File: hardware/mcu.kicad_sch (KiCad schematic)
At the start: 39 parts, among them J1 USB-C, SW3 RUN, SW4 BOOTSEL, U20 RP2350B, U21 GD25Q128ESIGR, U22 APS6404L-3SQR-SN, Y1 12MHz

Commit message: Plain address bytes in hardware; DVDD spine and bottom-row fan pre-routed
U1 delivers A0-A7 and U2 A8-A15 on MD0-MD7 (U2 over its fingers, U1 in the row
above fed from both sides), so the firmware sees ordinary addresses. preroute.py
now also fixes the DVDD spine under the package, the inner 3.3 V supply links,
pin 51's capacitor and a deterministic fan for the fully used bottom pad row.
OLED_DC moves to GP34. Exposed pad gets five ground vias. finish.py: DVDD first,
clearance-aware widening, hairline fixes, unused-via cleanup, overlapping pads.
Fully routed, zero DRC errors; fab outputs regenerated.

Co-Authored-By: Claude Fable 5.1 <noreply@anthropic.com>
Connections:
- net OLED_DC: now also U20.43 (GPIO34); no longer U20.49 (GPIO40/ADC0)
- net nAEN_X renamed nAEN_LO
- net nAEN_Y renamed nAEN_HI
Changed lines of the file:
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@@
   (global_label "MD6" (shape bidirectional) (at 154.94 116.84 0) (effects (font (size 1.27 1.27)) (justify left)))
   (global_label "MD7" (shape bidirectional) (at 154.94 119.38 0) (effects (font (size 1.27 1.27)) (justify left)))
-  (global_label "nAEN_X" (shape output) (at 154.94 121.92 0) (effects (font (size 1.27 1.27)) (justify left)))
-  (global_label "nAEN_Y" (shape output) (at 154.94 124.46 0) (effects (font (size 1.27 1.27)) (justify left)))
+  (global_label "nAEN_LO" (shape output) (at 154.94 121.92 0) (effects (font (size 1.27 1.27)) (justify left)))
+  (global_label "nAEN_HI" (shape output) (at 154.94 124.46 0) (effects (font (size 1.27 1.27)) (justify left)))
   (global_label "nDATA_OE" (shape output) (at 154.94 127.00 0) (effects (font (size 1.27 1.27)) (justify left)))
   (global_label "BE_REQ" (shape output) (at 154.94 129.54 0) (effects (font (size 1.27 1.27)) (justify left)))
@@
   (global_label "SD_SCK" (shape output) (at 154.94 198.12 0) (effects (font (size 1.27 1.27)) (justify left)))
   (global_label "SD_MOSI" (shape output) (at 154.94 200.66 0) (effects (font (size 1.27 1.27)) (justify left)))
-  (global_label "OLED_DC" (shape output) (at 104.14 182.88 180) (effects (font (size 1.27 1.27)) (justify right)))
+  (global_label "OLED_DC" (shape output) (at 154.94 187.96 0) (effects (font (size 1.27 1.27)) (justify left)))
   (global_label "OLED_CS" (shape output) (at 104.14 185.42 180) (effects (font (size 1.27 1.27)) (justify right)))
   (global_label "OLED_SCK" (shape output) (at 104.14 187.96 180) (effects (font (size 1.27 1.27)) (justify right)))
@@
   (no_connect (at 154.94 180.34))
   (no_connect (at 154.94 185.42))
-  (no_connect (at 154.94 187.96))
+  (no_connect (at 104.14 182.88))
   (label "PSRAM_CS" (at 104.14 200.66 180) (effects (font (size 1.27 1.27)) (justify right bottom)))
   (label "DVDD" (at 142.24 93.98 90) (effects (font (size 1.27 1.27)) (justify left bottom)))

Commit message: v3 prototype 2: bus pull-ups, SD socket power switch, PSRAM footprint
Fixes from proto1 bring-up and issue #21:

- R14 2k2 from nBE (edge A29) to +5V_EDGE. The 74LVC06 only pulls /BE
  low; without a pull-up it rose too slowly and a RAM opcode fetch after
  a served byte read wrong bits. Same value as the bodge on board 1.
- R15-R17 10k pull-ups on GP8-GP10 (nAEN_LO, nAEN_HI, nDATA_OE). The
  RP2350 resets its pads with pull-downs, so in reset and BOOTSEL all
  three buffers were enabled and U1 and U2 both drove MD.
- U32 SY6280AAC current-limited switch on the SD socket's VDD (+3V3_SD),
  enabled from XL9555 P0.6 (SD_PWR_EN), held off by R43 until the
  firmware sets it; R42 15k sets 0.45 A. A card that latches up hits the
  limit instead of pulling +3V3 down and resetting the RP2350B, and a
  wedged card can be power-cycled. R34-R37 move to +3V3_SD so they cannot
  power a switched-off card; the detect pull-up R38 stays on +3V3.
  Firmware: power on after the detect switch reads a card and before any
  SPI; release the SD pins before powering off.
- U22 footprint SOIC-8 3.9 x 4.9 mm. The APS6404L-3SQR-SN is SOP-8
  150 mil (AP Memory package code SN); proto1 had the 208 mil footprint.
  Still DNP; ESP-PSRAM64H (Adafruit 4677) fits the same pads by hand.

Routed by flow.py on the first attempt, DRC clean at every severity
(2119 segments, 385 vias). ERC: the one pre-existing U4 warning only.
$14.90/board at 10 with fees. PSRAM options surveyed in
docs/bom-cost-optimization.md.

Co-Authored-By: Claude Opus 5.5 <noreply@anthropic.com>
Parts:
- U22: footprint Package_SO:SOIC-8_5.3x5.3mm_P1.27mm -> Package_SO:SOIC-8_3.9x4.9mm_P1.27mm
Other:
- note added: "U21 boot flash (XIP CS0). U22 PSRAM on the same QSPI bus, DNP (fit APS6404L-3SQR-SN or ESP-PSRAM64H; SD-image cache only),"
- note removed: "U21 boot flash (XIP CS0). U22 PSRAM on the same QSPI bus, DNP on the prototype ($5 part, SD-image cache only),"
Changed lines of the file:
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@@
     (property "Reference" "U22" (at 343.36 182.19 0) (effects (font (size 1.27 1.27)) (justify left)))
     (property "Value" "APS6404L-3SQR-SN" (at 343.36 184.69 0) (effects (font (size 1.27 1.27)) (justify left)))
-    (property "Footprint" "Package_SO:SOIC-8_5.3x5.3mm_P1.27mm" (at 340.36 199.39 0) (effects (font (size 1.27 1.27)) (justify left) (hide yes)))
+    (property "Footprint" "Package_SO:SOIC-8_3.9x4.9mm_P1.27mm" (at 340.36 199.39 0) (effects (font (size 1.27 1.27)) (justify left) (hide yes)))
     (property "Datasheet" "" (at 340.36 199.39 0) (effects (font (size 1.27 1.27)) (justify left) (hide yes)))
     (property "Description" "" (at 340.36 199.39 0) (effects (font (size 1.27 1.27)) (justify left) (hide yes)))
@@
   (label "+3V3" (at 394.97 146.05 90) (effects (font (size 1.27 1.27)) (justify left bottom)))
   (label "nQSPI_SS" (at 394.97 153.67 270) (effects (font (size 1.27 1.27)) (justify right bottom)))
-  (text "U21 boot flash (XIP CS0). U22 PSRAM on the same QSPI bus, DNP on the prototype ($5 part, SD-image cache only)," (exclude_from_sim no) (at 320 225 0) (effects (font (size 1.5 1.5)) (justify left bottom)))
+  (text "U21 boot flash (XIP CS0). U22 PSRAM on the same QSPI bus, DNP (fit APS6404L-3SQR-SN or ESP-PSRAM64H; SD-image cache only)," (exclude_from_sim no) (at 320 225 0) (effects (font (size 1.5 1.5)) (justify left bottom)))
   (text "CS1 = GPIO47 (QMI CS1n). C37/C38 at U21/U22." (exclude_from_sim no) (at 320 228 0) (effects (font (size 1.5 1.5)) (justify left bottom)))
   (symbol (lib_id "Device:R") (at 250.19 209.55 0) (unit 1)

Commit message: v3 proto2: fit L1 by hand (not stocked at JLCPCB)
The RP2350 core-regulator inductor, Abracon AOTA-B201610S3R3-101-T,
was out of stock at JLCPCB and LCSC on 2026-10-12. Raspberry Pi's
design guide names no substitute (it is the only polarity-marked 0806
part, made for them), so L1 is DNP in the JLCPCB order and fitted by
hand from DigiKey/Mouser stock: dot on pad 2 (DVDD), the end away from
the board's top edge.

Only L1's DNP attribute changes in the board file; no routing touched.
Gerbers identical to v3.0-proto2 apart from date stamps; the BOM and
placement file lose L1 (39 lines, 139 parts). Also corrects the parts
table note, which had the dot on pin 1.

Co-Authored-By: Claude Opus 5.5 <noreply@anthropic.com>
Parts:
- L1: now not fitted
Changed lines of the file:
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@@
   (label "nQSPI_SS" (at 104.14 134.62 180) (effects (font (size 1.27 1.27)) (justify right bottom)))
   (symbol (lib_id "Device:L") (at 250.19 59.69 0) (unit 1)
-    (exclude_from_sim no) (in_bom yes) (on_board yes) (dnp no)
+    (exclude_from_sim no) (in_bom yes) (on_board yes) (dnp yes)
     (property "Reference" "L1" (at 253.19 51.38 0) (effects (font (size 1.27 1.27)) (justify left)))
     (property "Value" "3.3uH" (at 253.19 53.88 0) (effects (font (size 1.27 1.27)) (justify left)))

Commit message: v3 proto3: male DE-9, I2C OLED header, buttons in a 2x2 block
- J5: male DE-9 (CONNFLY DS1037-09MNAKT74-0CC, C75750). Atari sticks end
  in a female plug; proto1/2's female footprint mirrors every pin under a
  male part, putting the stick's ground on pin 7 (JOY_5V, open), so nothing
  read. Same body position and mounting holes as proto2.
- J3: 1x4 header for a 1.54in 128x64 SSD1309 I2C module (1 GND, 2 +3V3,
  3 SCL GP43, 4 SDA GP42) on I2C1, R44/R45 4k7 pull-ups. Replaces the 7-pin
  SSD1351 SPI header; GP34, GP41 and expander P0.2 (with R11) are freed.
- SW3 under SW1, SW4 under SW2, so the module covers no buttons; D4/R5
  move left of the ESP32, between H1 and the USB-C socket.

Routed by flow.py on the first attempt: DRC clean at every severity,
2125 segments, 373 vias. ERC: the one existing U4 warning.

Co-Authored-By: Claude Opus 5.5 <noreply@anthropic.com>
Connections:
- net OLED_CS: no longer names the net of U20.52 (GPIO41/ADC1)
- net OLED_DC: no longer names the net of U20.43 (GPIO34)
- net OLED_MOSI renamed OLED_SCL
- net OLED_SCK renamed OLED_SDA
- no-connect marks 9 -> 12
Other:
- note added: "RP2350B core per the RP2350 hardware design guide. GPIO map: docs/v3-architecture.md section 7. GP34, GP36, GP40, GP41 spare (plus the DMA pins when the DMA option is off)."
- note removed: "RP2350B core per the RP2350 hardware design guide. GPIO map: docs/v3-architecture.md section 7. GP36 spare (plus the six DMA pins when the DMA option is off)."
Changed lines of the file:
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@@
   (paper "A3")
   (title_block (title "TS-Pico v3: RP2350B Core") (rev "0.1") (company "Timex/Sinclair Online User Group"))
-  (text "RP2350B core per the RP2350 hardware design guide. GPIO map: docs/v3-architecture.md section 7. GP36 spare (plus the six DMA pins when the DMA option is off)." (exclude_from_sim no) (at 20 285 0) (effects (font (size 2.5 2.5)) (justify left bottom)))
+  (text "RP2350B core per the RP2350 hardware design guide. GPIO map: docs/v3-architecture.md section 7. GP34, GP36, GP40, GP41 spare (plus the DMA pins when the DMA option is off)." (exclude_from_sim no) (at 20 285 0) (effects (font (size 2.5 2.5)) (justify left bottom)))
   (text "USB-C: data, and VBUS to the power sheet (diode-ORed with the edge +5V) so the card runs from USB alone on the bench." (exclude_from_sim no) (at 20 290 0) (effects (font (size 2.0 2.0)) (justify left bottom)))
   (symbol (lib_id "power:+3V3") (at 299.72 30.48 0) (unit 1)
@@
   (global_label "SD_SCK" (shape output) (at 154.94 198.12 0) (effects (font (size 1.27 1.27)) (justify left)))
   (global_label "SD_MOSI" (shape output) (at 154.94 200.66 0) (effects (font (size 1.27 1.27)) (justify left)))
-  (global_label "OLED_DC" (shape output) (at 154.94 187.96 0) (effects (font (size 1.27 1.27)) (justify left)))
-  (global_label "OLED_CS" (shape output) (at 104.14 185.42 180) (effects (font (size 1.27 1.27)) (justify right)))
-  (global_label "OLED_SCK" (shape output) (at 104.14 187.96 180) (effects (font (size 1.27 1.27)) (justify right)))
-  (global_label "OLED_MOSI" (shape output) (at 104.14 190.50 180) (effects (font (size 1.27 1.27)) (justify right)))
+  (global_label "OLED_SDA" (shape bidirectional) (at 104.14 187.96 180) (effects (font (size 1.27 1.27)) (justify right)))
+  (global_label "OLED_SCL" (shape output) (at 104.14 190.50 180) (effects (font (size 1.27 1.27)) (justify right)))
   (global_label "WIFI_TX" (shape output) (at 104.14 193.04 180) (effects (font (size 1.27 1.27)) (justify right)))
   (global_label "WIFI_RX" (shape input) (at 104.14 195.58 180) (effects (font (size 1.27 1.27)) (justify right)))
@@
   (no_connect (at 154.94 180.34))
   (no_connect (at 154.94 185.42))
+  (no_connect (at 154.94 187.96))
+  (no_connect (at 154.94 187.96))
   (no_connect (at 104.14 182.88))
+  (no_connect (at 104.14 185.42))
   (label "PSRAM_CS" (at 104.14 200.66 180) (effects (font (size 1.27 1.27)) (justify right bottom)))
   (label "DVDD" (at 142.24 93.98 90) (effects (font (size 1.27 1.27)) (justify left bottom)))

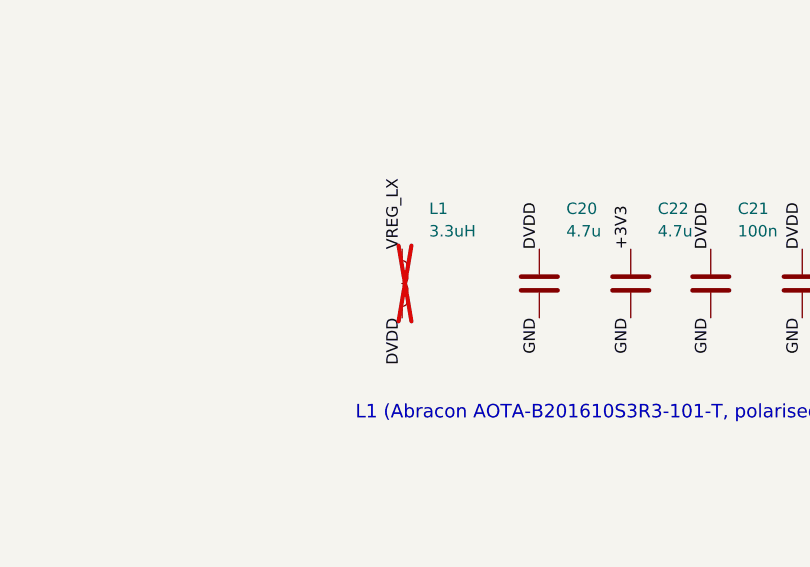
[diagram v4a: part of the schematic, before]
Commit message: v3 proto3.1: proto3 with board labels, L1 assembled again
Same copper as v3.0-proto3: copper, mask, paste, outline and drill
Gerbers are identical; only the two silkscreen layers differ, carrying
the board name, repository URL, licence and OSHW logo added on main
(labels.py, a875e92).

L1 (Abracon AOTA-B201610S3R3-101-T) is back in the JLCPCB BOM and
placement: 326 in stock on 2026-10-22, after being out of stock on
2026-10-12 (proto2.1 and proto3 hand-fitted it). Only L1's DNP flag
changes in the schematic and board; no routing touched. The fab notes
say to recheck its stock at upload and to fall back to hand-fitting.
U22 (PSRAM) stays hand-fitted.

DRC clean at every severity; ERC: the one U4 warning since proto1.
BOM 40 lines, 141 parts; $14.68/board at 10 with fees.

Co-Authored-By: Claude Opus 5.5 <noreply@anthropic.com>
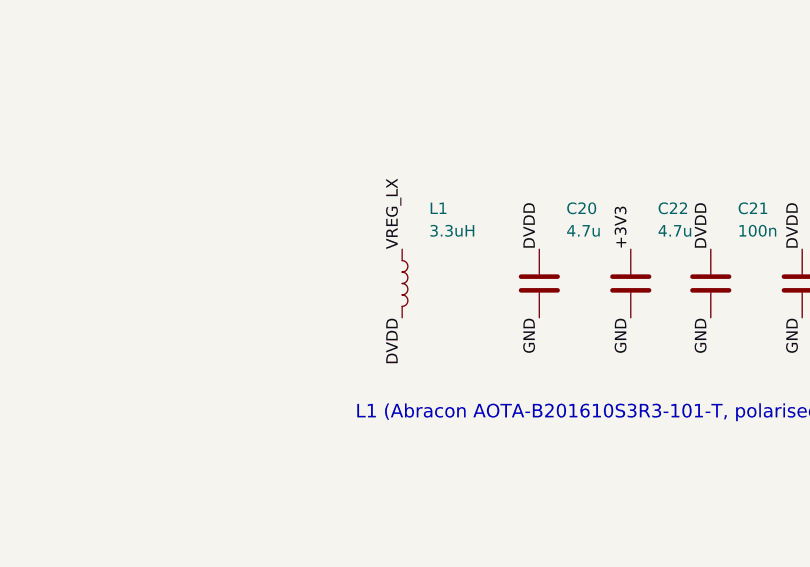
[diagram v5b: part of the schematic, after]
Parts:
- L1: now fitted
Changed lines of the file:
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@@
   (label "nQSPI_SS" (at 104.14 134.62 180) (effects (font (size 1.27 1.27)) (justify right bottom)))
   (symbol (lib_id "Device:L") (at 250.19 59.69 0) (unit 1)
-    (exclude_from_sim no) (in_bom yes) (on_board yes) (dnp yes)
+    (exclude_from_sim no) (in_bom yes) (on_board yes) (dnp no)
     (property "Reference" "L1" (at 253.19 51.38 0) (effects (font (size 1.27 1.27)) (justify left)))
     (property "Value" "3.3uH" (at 253.19 53.88 0) (effects (font (size 1.27 1.27)) (justify left)))
